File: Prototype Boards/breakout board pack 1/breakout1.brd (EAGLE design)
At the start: 50 x 50 mm, 14 parts, among them IC1 74LS151D, IC2 74LS03D, Q1 BCX70SMD

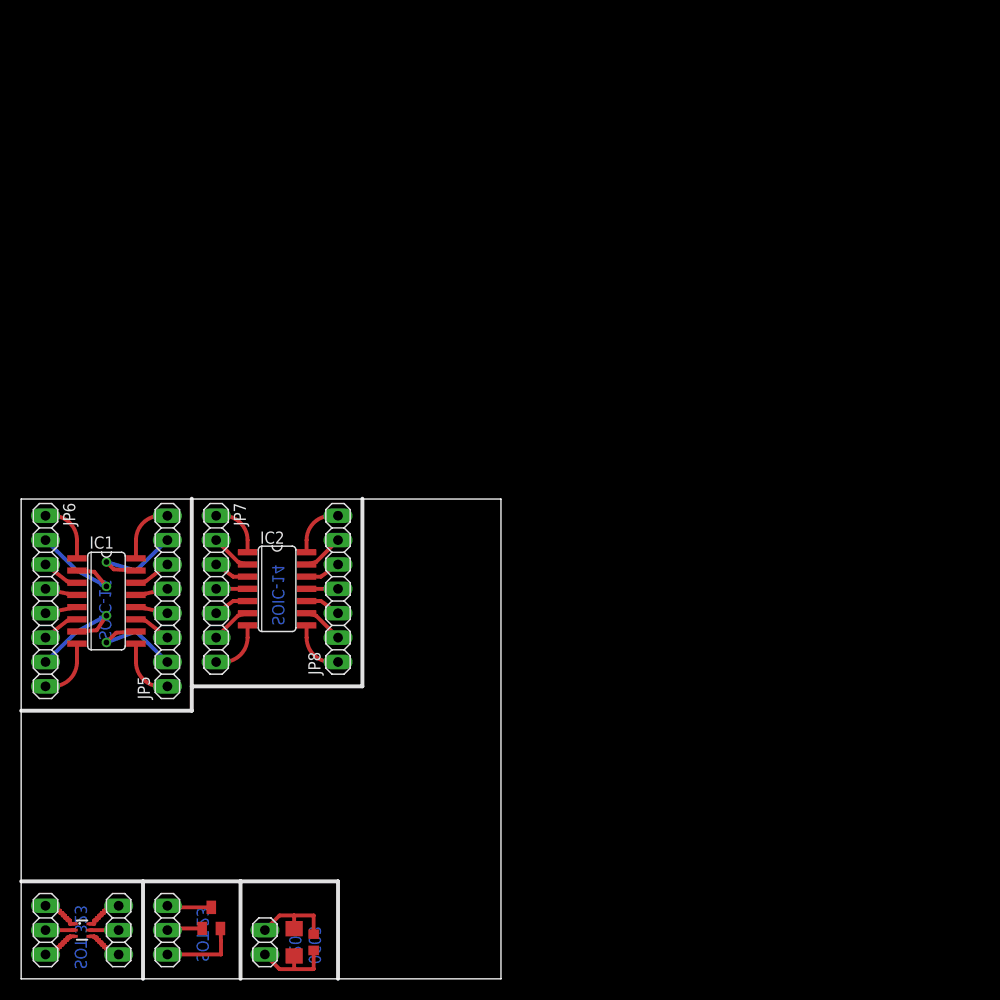
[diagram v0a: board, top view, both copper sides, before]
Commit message: finished laying out the breakout board. going to order this soon.
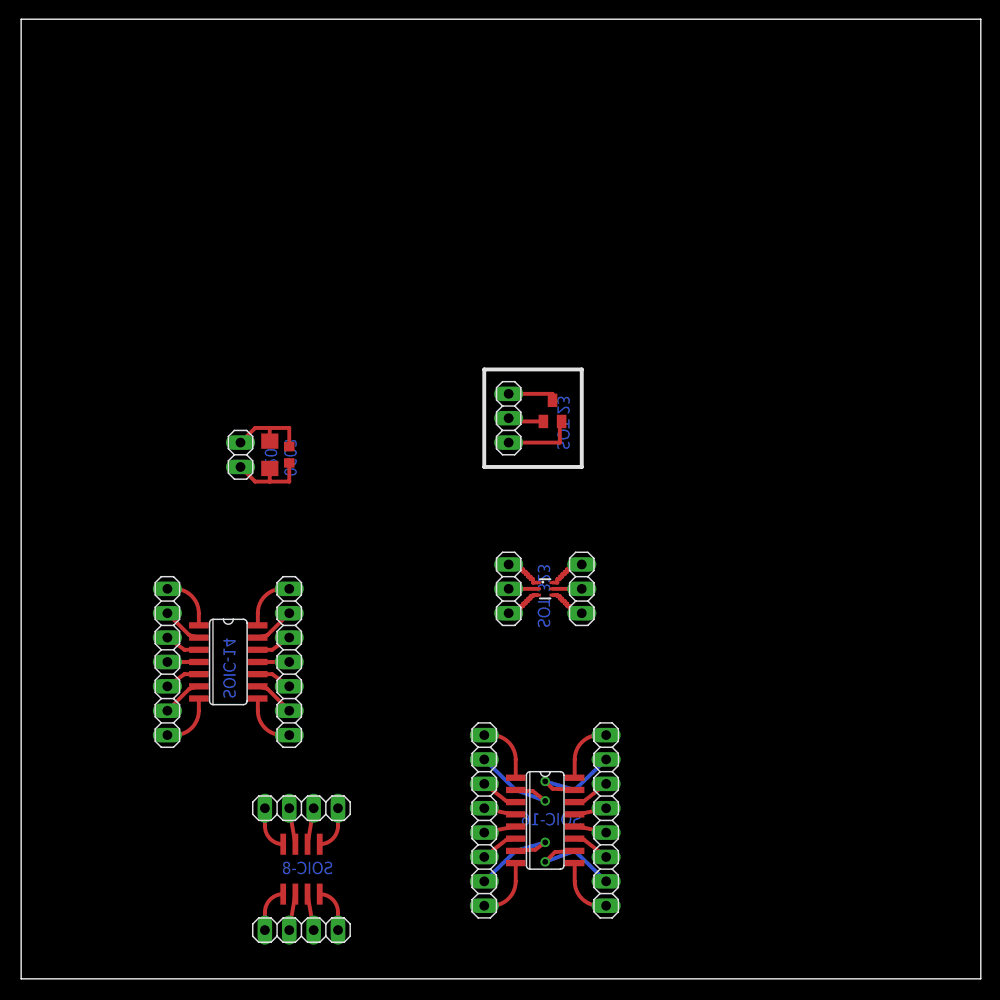
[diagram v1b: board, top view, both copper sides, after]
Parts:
- added IC3: NE555D, linear:SO08
- added JP10, JP9: (no value), pinhead:1X04
- moved JP3 64.1 mm to (50.8, 58.4)
- moved Q1 63.7 mm to (55.4, 59.2)
- moved JP1 59.9 mm to (50.8, 40.6)
- moved JP2 59.9 mm to (58.4, 40.6)
- moved U$1 59.9 mm to (54.6, 40.6)
- moved IC1 51.1 mm to (54.6, 16.5)
- moved JP5 51.1 mm to (61.0, 16.5)
- moved JP6 51.1 mm to (48.3, 16.5)
- moved JP4 50.9 mm to (22.9, 54.6)
- moved R2 50.9 mm to (27.9, 54.6)
- moved R4 50.9 mm to (25.9, 54.6)
- moved IC2 9.16 mm to (21.6, 33.0)
- moved JP8 9.16 mm to (27.9, 33.0)
- moved JP7 9.16 mm to (15.2, 33.0)
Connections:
- new net N$44: IC3.1, JP9.1
- new net N$45: IC3.2, JP9.2
- new net N$46: IC3.4, JP9.4
- new net N$47: IC3.3, JP9.3
- new net N$48: IC3.5, JP10.1
- new net N$49: IC3.6, JP10.2
- new net N$50: IC3.7, JP10.3
- new net N$51: IC3.8, JP10.4
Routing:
- net N$48: track 0.00 -> 4.54 mm
- net N$46: track 0.00 -> 4.54 mm
- net N$51: track 0.00 -> 4.54 mm
- net N$44: track 0.00 -> 4.54 mm
- net N$49: track 0.00 -> 3.80 mm
- net N$50: track 0.00 -> 3.80 mm
- net N$47: track 0.00 -> 3.80 mm
- net N$45: track 0.00 -> 3.80 mm
- net N$17: track 11.9 -> 11.1 mm
- net N$10: track 8.30 -> 7.72 mm
- net N$14: track 11.8 -> 11.3 mm
- net N$53: track 4.74 -> 5.25 mm
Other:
- board size 50 x 50 mm -> 100 x 100 mm
- board text added: "C B E"
- board text added: "SOIC-8"

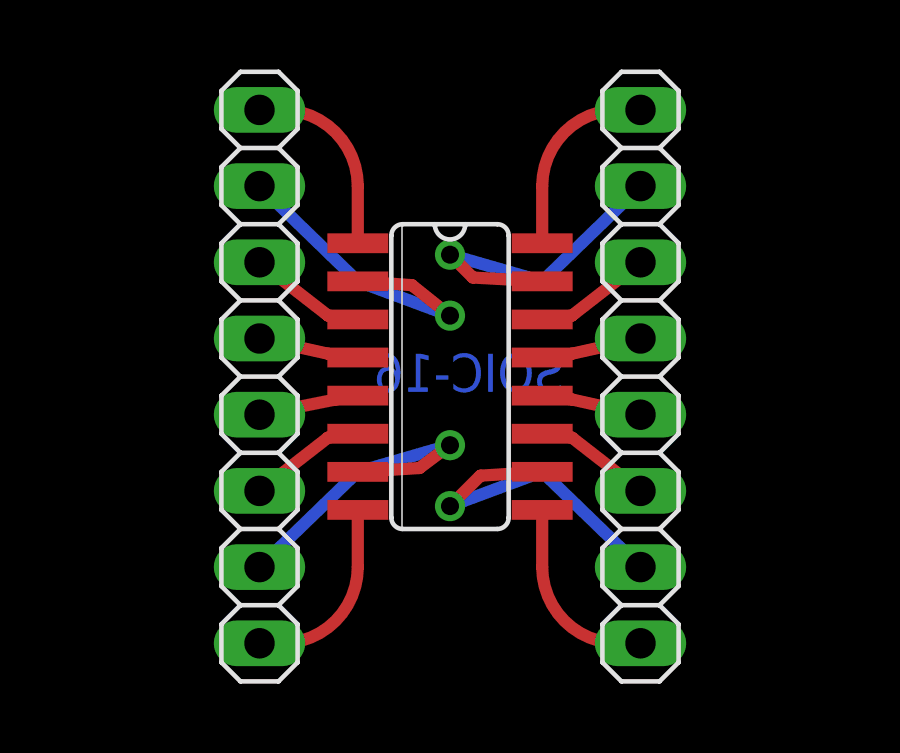
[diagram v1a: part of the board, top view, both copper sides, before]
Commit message: prototype board gerbers; ScreamFilter
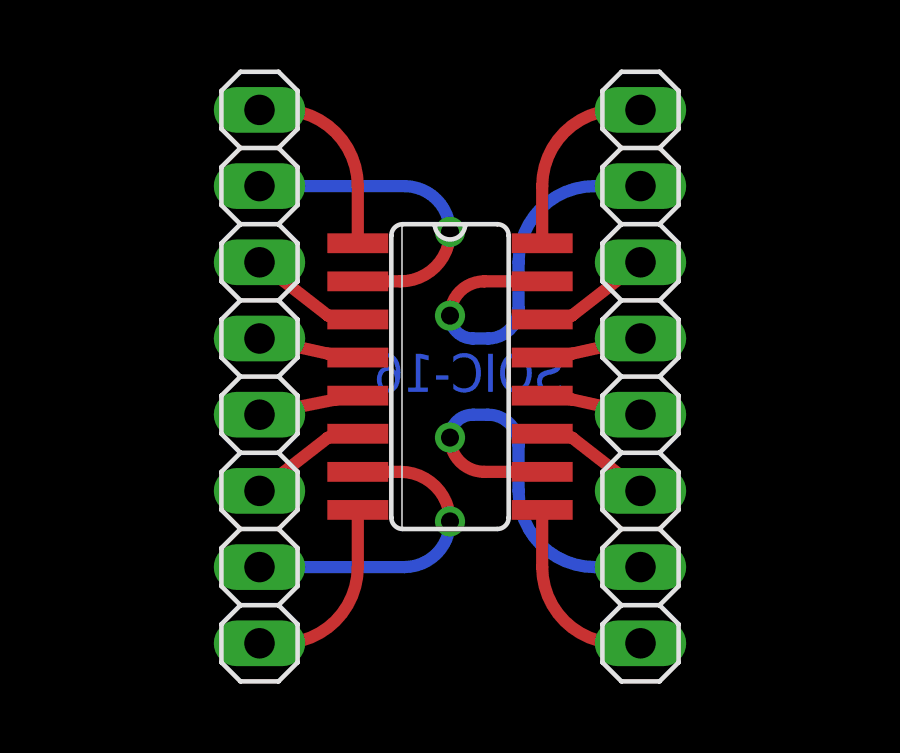
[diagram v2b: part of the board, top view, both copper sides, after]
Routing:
- net N$27: track 11.2 -> 13.2 mm
- net N$22: track 11.3 -> 13.2 mm
- net N$14: track 11.3 -> 10.7 mm
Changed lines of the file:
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@@
 <?xml version="1.0" encoding="utf-8"?>
 <!DOCTYPE eagle SYSTEM "eagle.dtd">
-<eagle version="7.6.0">
+<eagle version="6.6.0">
 <drawing>
 <settings>
@@
 <setting verticaltext="up"/>
 </settings>
-<grid distance="0.1" unitdist="inch" unit="mm" style="lines" multiple="1" display="no" altdistance="0.01" altunitdist="inch" altunit="mm"/>
+<grid distance="0.1" unitdist="inch" unit="inch" style="lines" multiple="1" display="no" altdistance="0.01" altunitdist="inch" altunit="inch"/>
 <layers>
 <layer number="1" name="Top" color="4" fill="1" visible="yes" active="yes"/>
@@
 <pass name="Default">
 <param name="RoutingGrid" value="50mil"/>
-<param name="AutoGrid" value="1"/>
-<param name="Efforts" value="0"/>
-<param name="TopRouterVariant" value="1"/>
 <param name="tpViaShape" value="round"/>
 <param name="PrefDir.1" value="|"/>
@@
 <contactref element="IC1" pad="2"/>
 <contactref element="JP6" pad="2"/>
-<wire x1="48.26" y1="22.86" x2="51.5366" y2="19.685" width="0.4064" layer="16"/>
-<wire x1="51.5366" y1="19.685" x2="54.61" y2="18.542" width="0.4064" layer="16"/>
-<via x="54.61" y="18.542" extent="1-16" drill="0.6" shape="square"/>
-<wire x1="54.61" y1="18.542" x2="53.34" y2="19.558" width="0.4064" layer="1"/>
-<wire x1="53.34" y1="19.558" x2="51.5366" y2="19.685" width="0.4064" layer="1"/>
+<wire x1="51.5366" y1="19.685" x2="52.959" y2="19.685" width="0.4064" layer="1"/>
+<wire x1="52.959" y1="19.685" x2="54.61" y2="21.336" width="0.4064" layer="1" curve="90"/>
+<via x="54.61" y="21.336" extent="1-16" drill="0.6" shape="square"/>
+<wire x1="54.61" y1="21.336" x2="53.086" y2="22.86" width="0.4064" layer="16" curve="90"/>
+<wire x1="53.086" y1="22.86" x2="48.26" y2="22.86" width="0.4064" layer="16"/>
 </signal>
 <signal name="N$15">
@@
 <contactref element="IC1" pad="7"/>
 <contactref element="JP6" pad="7"/>
-<wire x1="48.26" y1="10.16" x2="51.5366" y2="13.335" width="0.4064" layer="16"/>
-<wire x1="51.5366" y1="13.335" x2="54.61" y2="14.224" width="0.4064" layer="16"/>
-<via x="54.61" y="14.224" extent="1-16" drill="0.6" shape="square"/>
-<wire x1="54.61" y1="14.224" x2="53.594" y2="13.462" width="0.4064" layer="1"/>
-<wire x1="53.594" y1="13.462" x2="51.5366" y2="13.335" width="0.4064" layer="1"/>
+<wire x1="51.5366" y1="13.335" x2="52.959" y2="13.335" width="0.4064" layer="1"/>
+<wire x1="52.959" y1="13.335" x2="54.61" y2="11.684" width="0.4064" layer="1" curve="-90"/>
+<via x="54.61" y="11.684" extent="1-16" drill="0.6" shape="square"/>
+<wire x1="54.61" y1="11.684" x2="53.086" y2="10.16" width="0.4064" layer="16" curve="-90"/>
+<wire x1="53.086" y1="10.16" x2="48.26" y2="10.16" width="0.4064" layer="16"/>
 </signal>
 <signal name="N$18">
@@
 <contactref element="IC1" pad="10"/>
 <contactref element="JP5" pad="2"/>
-<wire x1="60.96" y1="10.16" x2="57.6834" y2="13.335" width="0.4064" layer="16"/>
-<wire x1="57.6834" y1="13.335" x2="54.61" y2="12.192" width="0.4064" layer="16"/>
-<via x="54.61" y="12.192" extent="1-16" drill="0.6" shape="square"/>
-<wire x1="54.61" y1="12.192" x2="55.626" y2="13.208" width="0.4064" layer="1"/>
-<wire x1="55.626" y1="13.208" x2="57.6834" y2="13.335" width="0.4064" layer="1"/>
+<wire x1="57.6834" y1="13.335" x2="55.753" y2="13.335" width="0.4064" layer="1"/>
+<wire x1="55.753" y1="13.335" x2="54.61" y2="14.478" width="0.4064" layer="1" curve="-90"/>
+<via x="54.61" y="14.478" extent="1-16" drill="0.6" shape="square"/>
+<wire x1="54.61" y1="14.478" x2="55.372" y2="15.24" width="0.4064" layer="16" curve="-90"/>
+<wire x1="55.372" y1="15.24" x2="55.88" y2="15.24" width="0.4064" layer="16"/>
+<wire x1="55.88" y1="15.24" x2="56.896" y2="14.224" width="0.4064" layer="16" curve="-90"/>
+<wire x1="56.896" y1="14.224" x2="56.896" y2="12.7" width="0.4064" layer="16"/>
+<wire x1="56.896" y1="12.7" x2="59.436" y2="10.16" width="0.4064" layer="16" curve="90"/>
+<wire x1="59.436" y1="10.16" x2="60.96" y2="10.16" width="0.4064" layer="16"/>
 </signal>
 <signal name="N$23">
@@
 <contactref element="IC1" pad="15"/>
 <contactref element="JP5" pad="7"/>
-<wire x1="60.96" y1="22.86" x2="57.6834" y2="19.685" width="0.4064" layer="16"/>
-<wire x1="57.6834" y1="19.685" x2="54.61" y2="20.574" width="0.4064" layer="16"/>
-<via x="54.61" y="20.574" extent="1-16" drill="0.6" shape="square"/>
-<wire x1="54.61" y1="20.574" x2="55.372" y2="19.812" width="0.4064" layer="1"/>
-<wire x1="55.372" y1="19.812" x2="57.6834" y2="19.685" width="0.4064" layer="1"/>
+<wire x1="57.6834" y1="19.685" x2="55.753" y2="19.685" width="0.4064" layer="1"/>
+<wire x1="55.753" y1="19.685" x2="54.61" y2="18.542" width="0.4064" layer="1" curve="90"/>
+<via x="54.61" y="18.542" extent="1-16" drill="0.6" shape="square"/>
+<wire x1="54.61" y1="18.542" x2="55.372" y2="17.78" width="0.4064" layer="16" curve="90"/>
+<wire x1="55.372" y1="17.78" x2="55.88" y2="17.78" width="0.4064" layer="16"/>
+<wire x1="55.88" y1="17.78" x2="56.896" y2="18.796" width="0.4064" layer="16" curve="90"/>
+<wire x1="56.896" y1="18.796" x2="56.896" y2="20.32" width="0.4064" layer="16"/>
+<wire x1="56.896" y1="20.32" x2="59.436" y2="22.86" width="0.4064" layer="16" curve="-90"/>
+<wire x1="59.436" y1="22.86" x2="60.96" y2="22.86" width="0.4064" layer="16"/>
 </signal>
 <signal name="N$29">
